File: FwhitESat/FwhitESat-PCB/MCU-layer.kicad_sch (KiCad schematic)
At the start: 1 part, among them U3 Pico

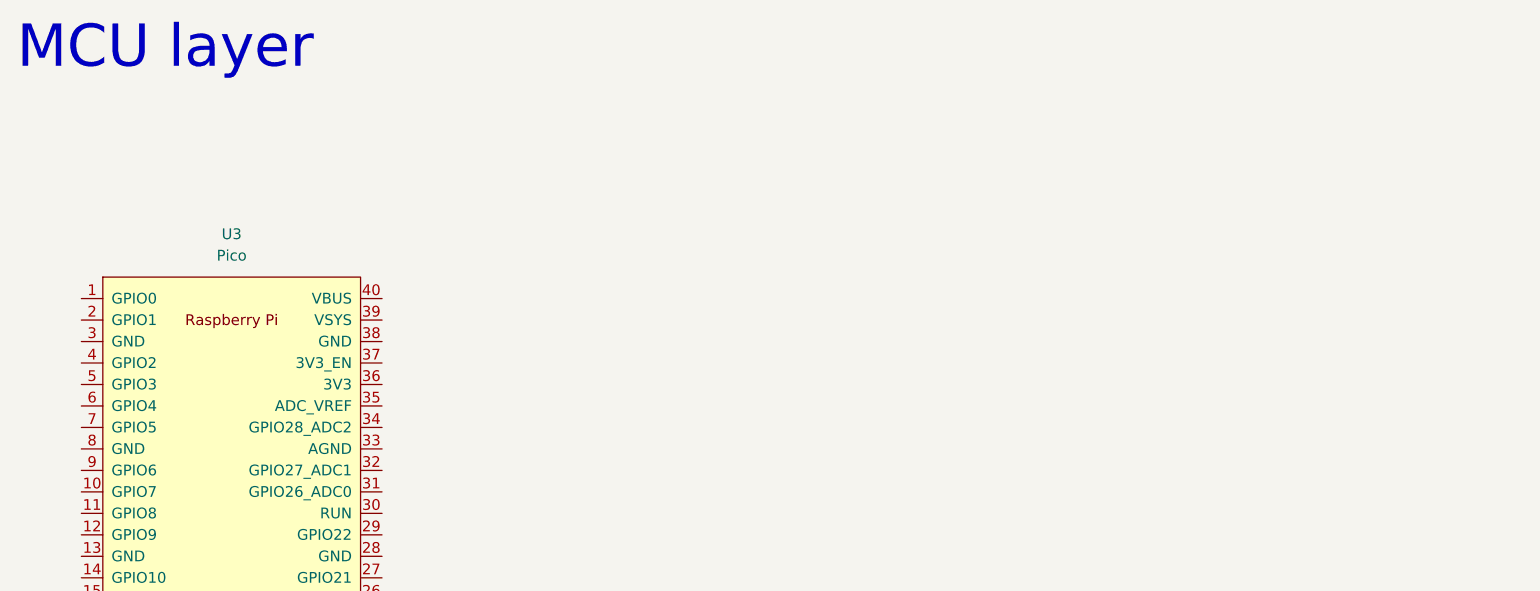
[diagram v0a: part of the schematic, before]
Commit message: fix FwhitESat/FwhitESat-PCB
add I2C line.
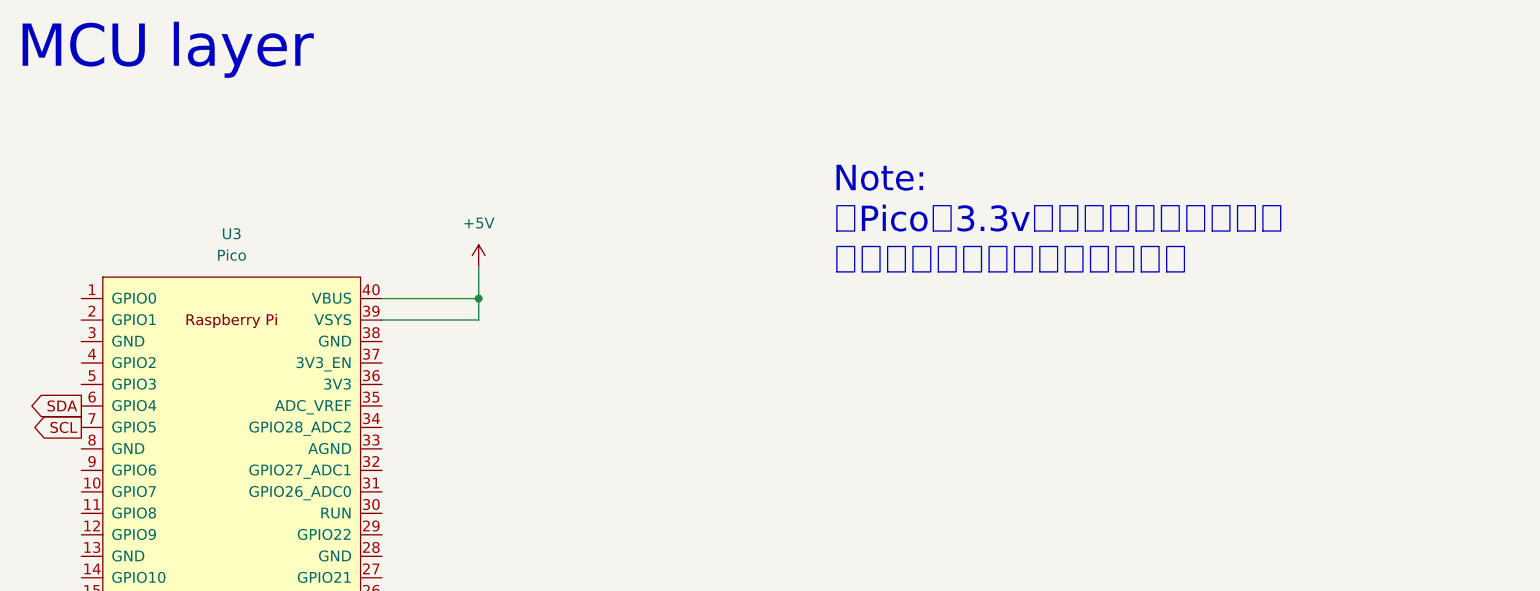
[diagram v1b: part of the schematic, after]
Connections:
- net +5V: now reaches U3.39 (VSYS)
- net +5V: now also U3.40 (VBUS)
- net SDA: now reaches U3.6 (GPIO4)
- net SCL: now reaches U3.7 (GPIO5)
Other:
- note added: "Note: Picoの3.3v出力は電流制限のため センサーの電源に使用しない。"
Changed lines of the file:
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@@
 (kicad_sch (version 20230121) (generator eeschema)
   (paper "A4")
+  (junction (at 132.08 59.69) (diameter 0) (color 0 0 0 0)
+  )
+  (wire (pts (xy 132.08 59.69) (xy 120.65 59.69))
+    (stroke (width 0) (type default))
+  )
+  (wire (pts (xy 120.65 62.23) (xy 132.08 62.23))
+    (stroke (width 0) (type default))
+  )
+  (wire (pts (xy 132.08 62.23) (xy 132.08 59.69))
+    (stroke (width 0) (type default))
+  )
+  (wire (pts (xy 132.08 55.88) (xy 132.08 59.69))
+    (stroke (width 0) (type default))
+  )
+  (text "Note:\n　Picoの3.3v出力は電流制限のため\nセンサーの電源に使用しない。" (at 173.99 57.15 0)
+    (effects (font (size 3 3)) (justify left bottom))
+  )
   (text "MCU layer" (at 77.47 33.02 0)
     (effects (font (size 5 5)) (justify left bottom))
+  )
+  (global_label "SCL" (shape output) (at 85.09 74.93 180) (fields_autoplaced)
+    (effects (font (size 1.27 1.27)) (justify right))
+    (property "Intersheetrefs" "${INTERSHEET_REFS}" (at 78.5972 74.93 0)
+      (effects (font (size 1.27 1.27)) (justify right) hide)
+    )
+  )
+  (global_label "SDA" (shape output) (at 85.09 72.39 180) (fields_autoplaced)
+    (effects (font (size 1.27 1.27)) (justify right))
+    (property "Intersheetrefs" "${INTERSHEET_REFS}" (at 78.5367 72.39 0)
+      (effects (font (size 1.27 1.27)) (justify right) hide)
+    )
   )
   (symbol (lib_id "01-FwhitESat-Local_Library:Pico") (at 102.87 83.82 0) (unit 1)
@@
         )
       )
+    )
+  )
+  (symbol (lib_id "power:+5V") (at 132.08 55.88 0) (unit 1)
+    (in_bom yes) (on_board yes) (dnp no) (fields_autoplaced)
+    (property "Reference" "#PWR05" (at 132.08 59.69 0)
+      (effects (font (size 1.27 1.27)) hide)
+    )
+    (property "Value" "+5V" (at 132.08 50.8 0)
+      (effects (font (size 1.27 1.27)))
+    )
+    (property "Footprint" "" (at 132.08 55.88 0)
+      (effects (font (size 1.27 1.27)) hide)
+    )
+    (property "Datasheet" "" (at 132.08 55.88 0)
+      (effects (font (size 1.27 1.27)) hide)
+    )
+    (pin "1")
+    (instances
+      (project "FwhitESat-PCB"
+        (path "/78ea2883-2db0-4d81-80e1-b63c1c2056ac"
+          (reference "#PWR05") (unit 1)
+        )
+        (path "/78ea2883-2db0-4d81-80e1-b63c1c2056ac/56957d94-f740-47f0-918d-81f554d7e663"
+          (reference "#PWR012") (unit 1)
+        )
+        (path "/78ea2883-2db0-4d81-80e1-b63c1c2056ac/f4665424-10ff-4a9f-9002-a506404d9567"
+          (reference "#PWR01") (unit 1)
+        )
+      )

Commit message: くっぱ
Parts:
- added C1: C, symbol 01-FwhitESat-Local_Library:C
- added D3: D_Schottky, symbol 01-FwhitESat-Local_Library:D_Schottky
- added J1: Micro_SD_Card, symbol 01-FwhitESat-Local_Library:Micro_SD_Card
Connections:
- net +5V: now also D3.2 (A); no longer U3.39 (VSYS), U3.40 (VBUS)
- net RasTX: now reaches U3.1 (GPIO0)
- net GND: now reaches U3.13 (GND)
- net GND: now also U3.18 (GND), U3.23 (GND), U3.28 (GND), U3.3 (GND), U3.33 (AGND), U3.38 (GND), U3.8 (GND), C1.2, J1.6 (VSS), J1.9 (SHIELD)
- net SPI1-MISO: now reaches U3.16 (GPIO12)
- net SPI1-MISO: now also J1.7 (DAT0)
- net SPI1-CS: now reaches U3.17 (GPIO13)
- net SPI1-CS: now also J1.2 (DAT3/CD)
- net SPI1-CLK: now reaches U3.19 (GPIO14)
- net SPI1-CLK: now also J1.5 (CLK)
- net RasRX: now reaches U3.2 (GPIO1)
- net SPI1-MOSI: now reaches U3.20 (GPIO15)
- net SPI1-MOSI: now also J1.3 (CMD)
- net PWRlamp: now reaches U3.21 (GPIO16)
- net Servolamp: now reaches U3.22 (GPIO17)
- new net: C1.1, D3.1 (K), U3.39 (VSYS)
- new net +3.3V: J1.4 (VDD)
- no-connect marks 0 -> 5
